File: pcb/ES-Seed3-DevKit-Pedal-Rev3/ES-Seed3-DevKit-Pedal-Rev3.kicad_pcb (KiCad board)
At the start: 2 copper layers, 197 x 100 mm, 152 parts, among them J1 DIN_MIDI_5P, J10 DIN_MIDI_5P, J11 DIN_MIDI_5P, J2 JACK_TRS_SWITCHING, J3 JACK_TRS_SWITCHING, J4 JACK_TRS_SWITCHING, J5 JACK_TRS_SWITCHING, J6 JACK_TRS_SWITCHING, J7 USB4110GFA, J8 Barrel_Jack_Switch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

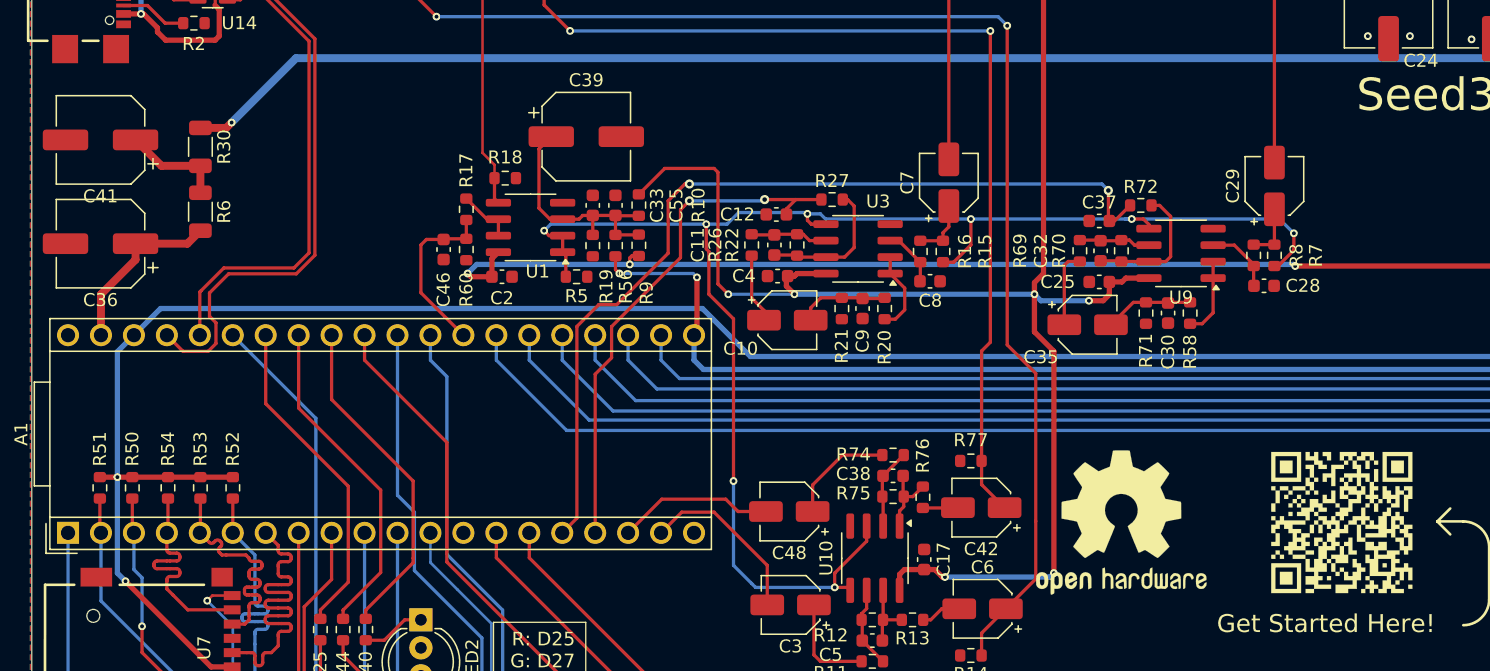
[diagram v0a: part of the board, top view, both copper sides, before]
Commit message: fixed QR code to be correct destination link, and removed DNIs.
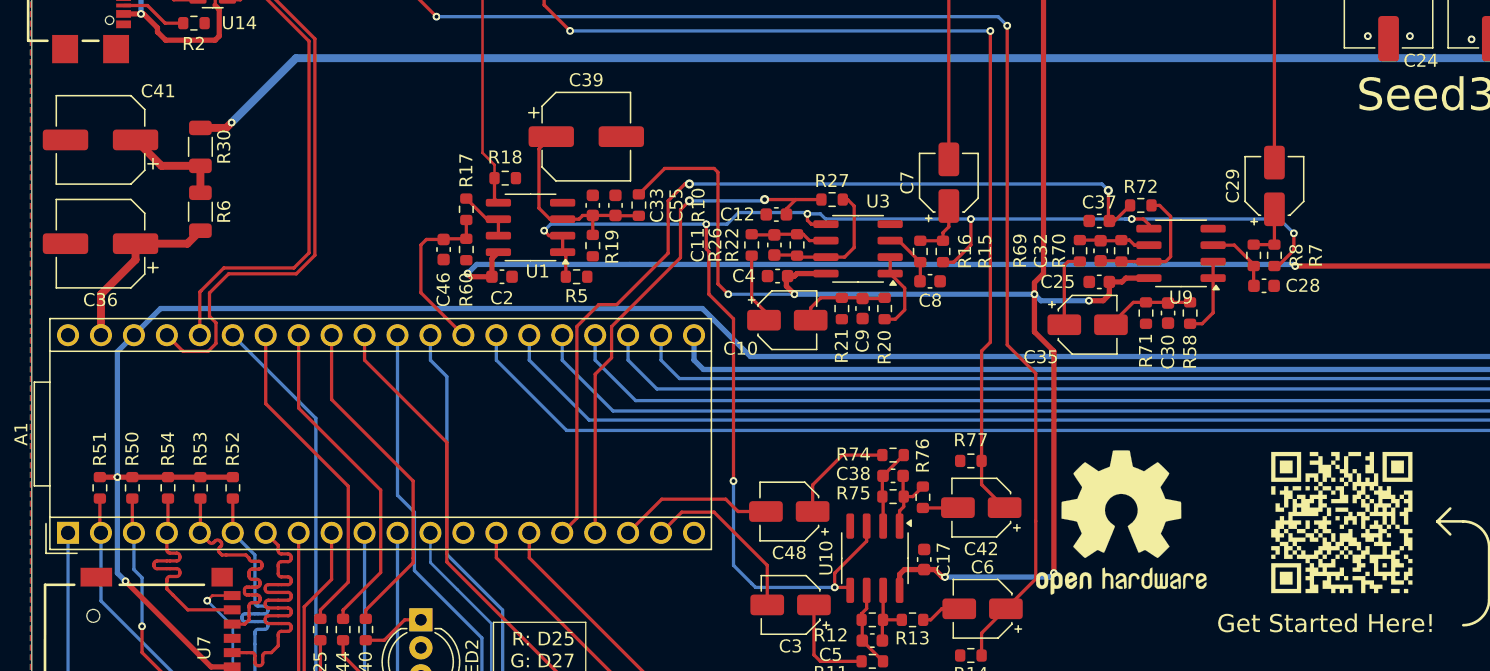
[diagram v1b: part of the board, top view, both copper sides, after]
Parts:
- removed R56: 10K, Resistor_SMD:R_0603_1608Metric
- removed R9: 0R, Resistor_SMD:R_0603_1608Metric
- QR1: footprint shnsly:qr-seed3-desktop-redirect-medium -> shnsly:qr-seed3-pedal-redirect-medium
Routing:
- net +3V3_A: track 196.1 -> 184.3 mm, vias 5 -> 3
- net Net-(U1A-+): track 19.3 -> 16.0 mm
- net +5V_A: track 171.3 -> 170.0 mm, vias 3 -> 2
